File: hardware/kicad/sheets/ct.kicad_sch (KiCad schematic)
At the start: 31 parts, among them J12 CT, J13 AC_SENSE_DNP, U7 ADE7953ACPZ, Y1 3.579545MHz XO

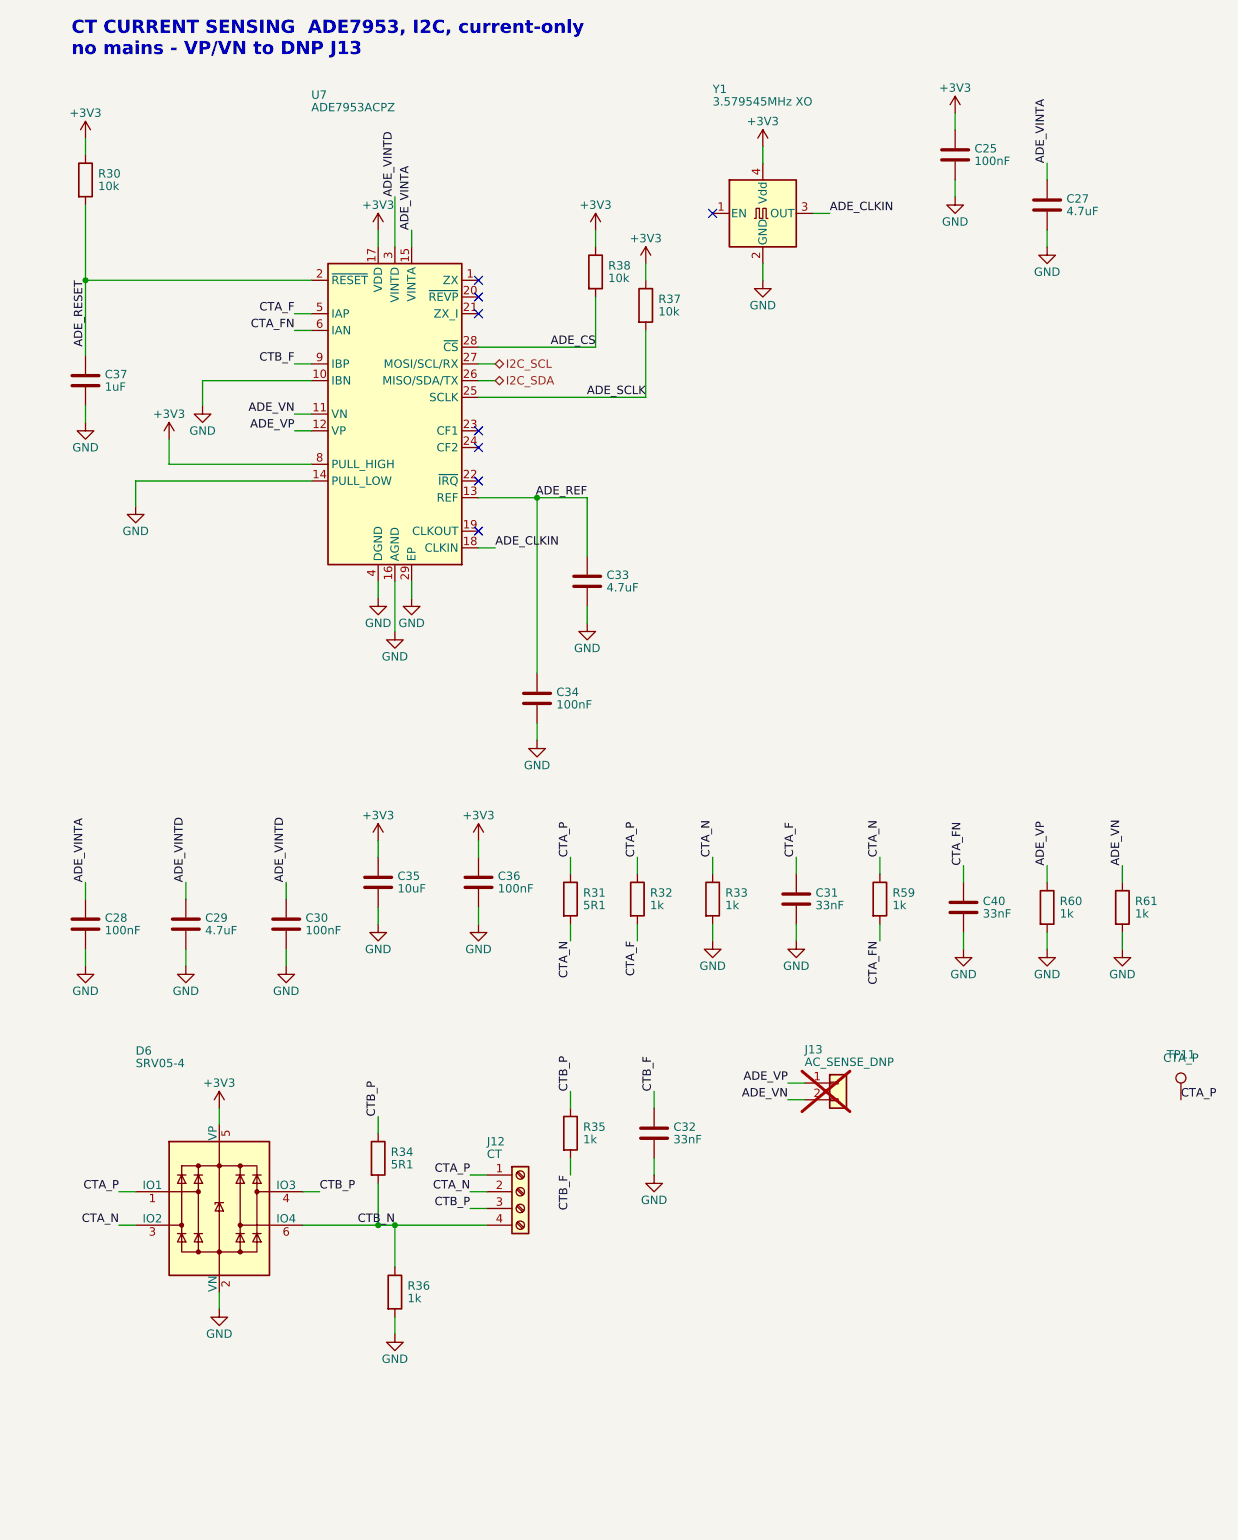
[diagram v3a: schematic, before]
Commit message: hardware: inline front-ends and decoupling at the pins (review 12, 13)
Fourth batch from SCHEMATIC-REVIEW-2026-10-22.md.

Thermocouples: each MAX31856 front-end is an inline chain - the terminal
mirrored so its pins face the IC, K+ and K- on two lines through their
100R, the 100 nF differential cap bridging the lines, the 10 nF caps to
GND off each line, BIAS returned to the raw K- node along the bottom -
and AVDD/DVDD rise to a short +3V3 rail with both 100 nF hanging from
it. The ICs slid 7.62 mm right to make room; nothing else moved.

CT: J12 feeds four lines at 17.78 mm pitch with the 5R1 burden between
each pair, the 1k series parts in the path, the 33 nF to GND off each
filtered node and the 1k references off the N lines; the filtered nodes
end in the CTA_F / CTA_FN / CTB_F labels the ADE7953 pins already
carried. D6 keeps a label-fed clamp block beside the chain. VDD, VINTD
and VINTA each get a rail at the IC's top pin with their two caps on it;
R37/R38 moved 7.62 mm right to clear them.

io: IN1-IN3 are three identical rows - J11 mirrored, 1k in the path, the
10k pull-up above and 100 nF below the node, the hierarchical label at
the end - with D5's clamp block below them.

mcu: C6/C7 hang from U1's 3V3 pin. power: U2 is drawn as an inline
5 V -> 3.3 V chain with C1/C2 on its input and C3/C4 on its output in
the row the caps already occupied; LED2/R9 slid right.

Every pin landed on wiring by construction (the geometry helper checks
each symbol's pins against the wires), ERC is clean, the layout checker
reports no overlaps, the netlist still has 108 nets and the board sync
re-netted nothing. Fab outputs regenerated (schematic PDF, timestamps).

Co-Authored-By: Claude Fable 5.1 <noreply@anthropic.com>
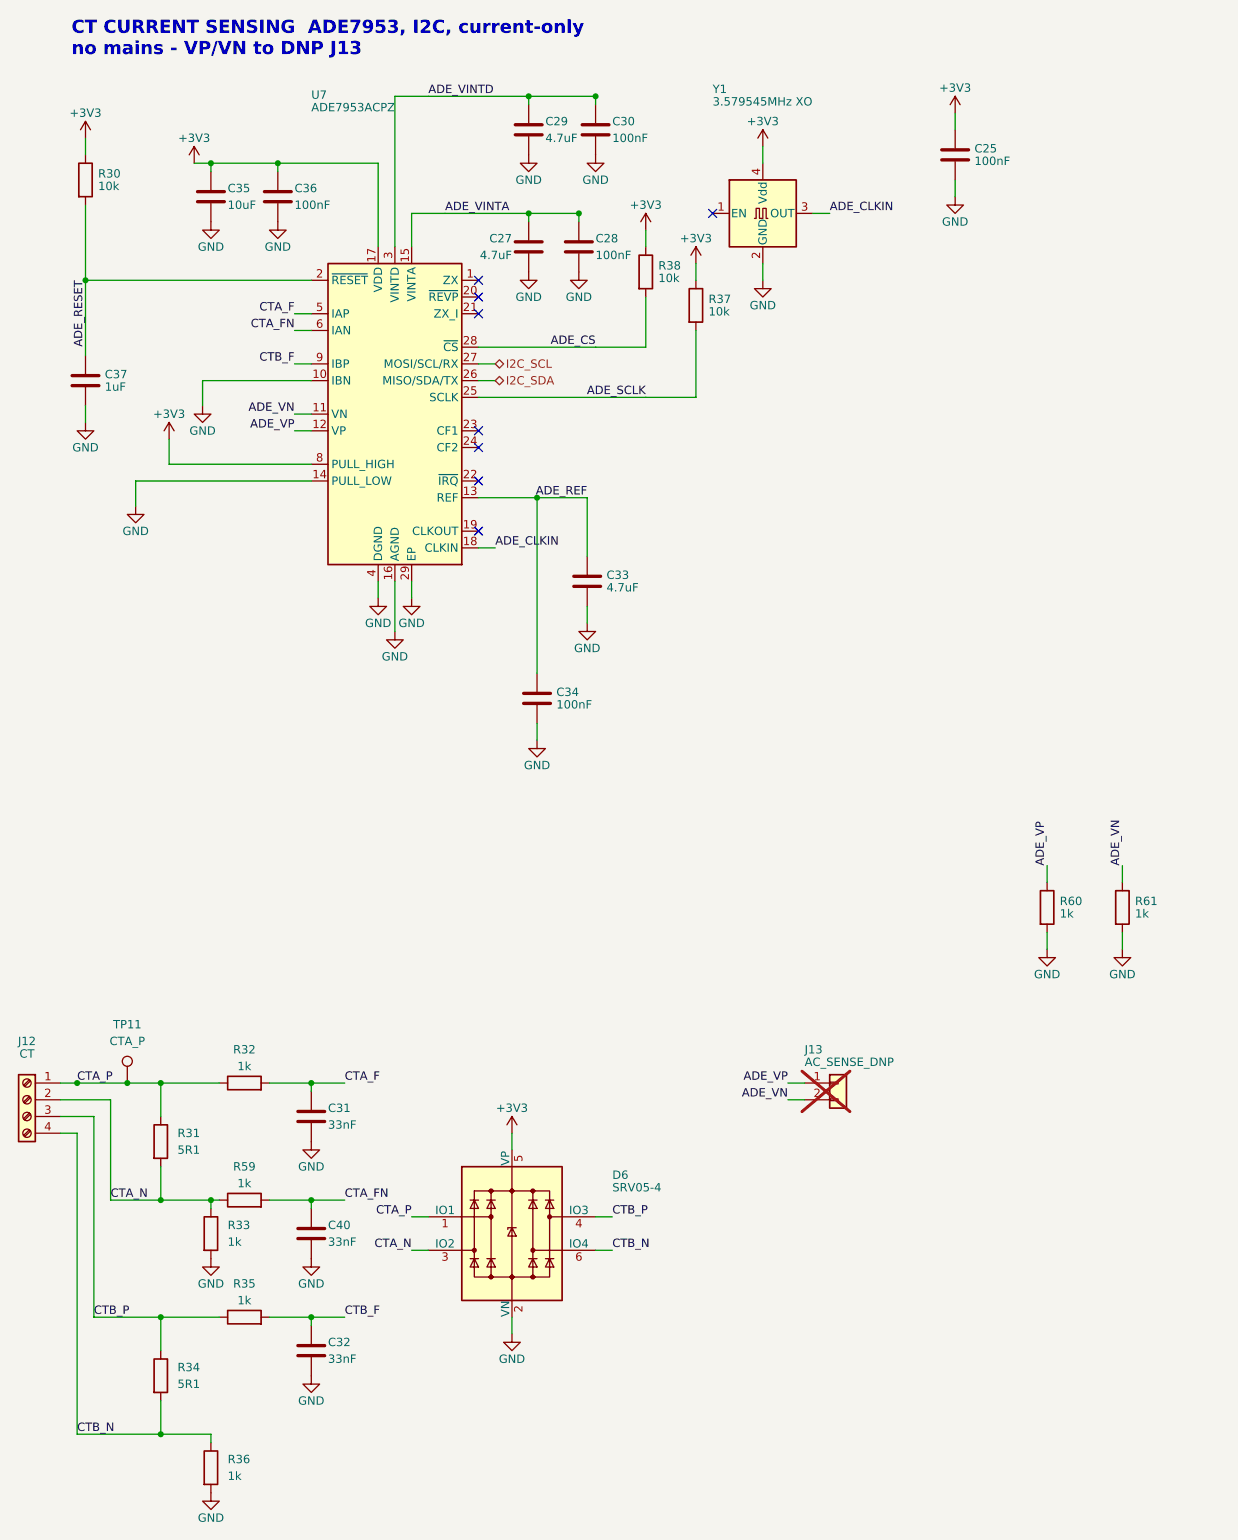
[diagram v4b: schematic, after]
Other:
- moved on the sheet: C27, C28, C29, C30, C31, C32, C35, C36, C40, D6, J12, R31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

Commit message: hardware: drop the five test points a connector already exposes
TP1 (+3V3), TP2 (+5V), TP7/TP8 (I2C) and TP11 (CTA_P) each sat on a net
that a connector pin already reaches: +3V3 and I2C on the J7 AUX header
and J14 QWIIC, +5V on J5 pin 1, CTA_P on J12 pin 1. They are gone from
the test, mcu and ct sheets (TP3 and TP9/TP10 slide left into the gaps),
the board is synced, and the copper that only existed to reach them is
removed: eight segments and one via, 15.5 mm in all, most of it +5V's
spur from U2.3 up to the old TP2. DRC is 0 violations / 0 unconnected
with every severity on.

The seven that remain (TP3-TP6, TP9, TP10, TP12) probe nets nothing else
reaches, and none moved: on the board each already sits inline on its
net's route with at most a 0.4 mm jog. TP12 is the one with a real stub
(3.3 mm from R46.2), and SJ2's courtyard is what keeps it there.

TP_LEGEND_OK is empty again - dropping TP11 was the way out review A2
named. README, the bench smoke test (rails now probed at C2 / J7 pin 1),
gen_jlc's not-assembled set and the datasheet manifest follow. ERC 0,
make pcb-check ALL CHECKS PASS, SYNC IDEMPOTENT: PASS; fab outputs and
3D renders regenerated.

Co-Authored-By: Claude Fable 5.1 <noreply@anthropic.com>
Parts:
- removed TP11: CTA_P, TestPoint:TestPoint_Pad_D1.0mm, symbol Connector:TestPoint
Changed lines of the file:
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@@
-	)
-	(junction
-		(at 30.48 187.96)
-		(diameter 0)
-		(color 0 0 0 0)
 	)
 	(junction
@@
 					(unit 1)
 				)
-			)
-		)
-	)
-	(symbol
-		(lib_id "Connector:TestPoint")
-		(at 30.48 187.96 0)
-		(unit 1)
-		(body_style 1)
-		(exclude_from_sim no)
-		(in_bom yes)
-		(on_board yes)
-		(in_pos_files yes)
-		(dnp no)
-		(property "Reference" "TP11"
-			(at 30.48 179.07 0)
-			(show_name no)
-			(do_not_autoplace no)
-			(effects
-				(font
-					(size 1.27 1.27)
-				)
-			)
-		)
-		(property "Value" "CTA_P"
-			(at 30.48 181.61 0)
-			(show_name no)
-			(do_not_autoplace no)
-			(effects
-				(font
-					(size 1.27 1.27)
-				)
-			)
-		)
-		(property "Footprint" "TestPoint:TestPoint_Pad_D1.0mm"
-			(at 30.48 187.96 0)
-			(hide yes)
-			(show_name no)
-			(do_not_autoplace no)
-			(effects
-				(font
-					(size 1.27 1.27)
-				)
-			)
-		)
-		(property "Datasheet" ""
-			(at 30.48 187.96 0)
-			(hide yes)
-			(show_name no)
-			(do_not_autoplace no)
-			(effects
-				(font
-					(size 1.27 1.27)
-				)
-			)
-		)
-		(property "Description" "test point"
-			(at 30.48 187.96 0)
-			(hide yes)
-			(show_name no)
-			(do_not_autoplace no)
-			(effects
-				(font
-					(size 1.27 1.27)
-				)
-			)
-		)
-		(pin "1"
-		)
-		(instances
-			(project ""
-				(path "/9f5a642e-6117-5c0b-a848-1913aa103515"
-					(reference "TP11")
-					(unit 1)
-				)

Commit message: hardware: drop J13, the DNP header on the ADE7953 voltage channel
True power measurement is not a planned feature, so the provision for a
future off-board isolated AC-sense accessory goes: J13 is removed from
the ct sheet, VP/VN stay held at GND by R60/R61 and reach nothing else,
and the sheet note says so. gen_jlc.DNP is empty; J13 leaves
NOT_ASSEMBLED, the silk legend tables and the datasheet manifest, and
README/DESIGN-NOTES no longer describe the header or the upgrade path.

On the board the header's two through-hole pads were also the layer
change in each net's route, so removing the footprint left ADE_VP and
ADE_VN each split between F.Cu and B.Cu. A 0.6/0.3 via now sits where
each pad was, and the zones are refilled around them. DRC 0 violations
/ 0 unconnected with every severity on, ERC 0, make pcb-check ALL
CHECKS PASS, SYNC IDEMPOTENT: PASS; fab outputs and 3D renders
regenerated.

Co-Authored-By: Claude Fable 5.1 <noreply@anthropic.com>
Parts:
- removed J13: AC_SENSE_DNP, Connector_PinHeader_2.54mm:PinHeader_1x02_P2.54mm_Vertical, symbol Connector_Generic:Conn_01x02
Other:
- note added: "CT CURRENT SENSING ADE7953, I2C, current-only no mains - VP/VN held at GND by R60/R61"
- note removed: "CT CURRENT SENSING ADE7953, I2C, current-only no mains - VP/VN to DNP J13"
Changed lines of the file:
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@@
 		(comment 2 "4-layer, 100 x 100 mm, JLCPCB standard process")
 	)
-	(text "CT CURRENT SENSING  ADE7953, I2C, current-only\nno mains - VP/VN to DNP J13"
+	(text "CT CURRENT SENSING  ADE7953, I2C, current-only\nno mains - VP/VN held at GND by R60/R61"
 		(exclude_from_sim no)
 		(at 22 29.4 0)
@@
 	(wire
 		(pts
-			(xy 133.35 187.96) (xy 130.81 187.96)
-		)
-		(stroke
-			(width 0)
-			(type default)
-		)
-	)
-	(wire
-		(pts
 			(xy 35.56 236.22) (xy 35.56 241.3)
 		)
@@
 	(wire
 		(pts
-			(xy 133.35 190.5) (xy 130.81 190.5)
-		)
-		(stroke
-			(width 0)
-			(type default)
-		)
-	)
-	(wire
-		(pts
 			(xy 58.42 93.98) (xy 36.83 93.98)
 		)
@@
 		)
 	)
-	(label "ADE_VP"
-		(at 130.81 187.96 180)
-		(effects
-			(font
-				(size 1.27 1.27)
-			)
-			(justify right bottom)
-		)
-	)
 	(label "ADE_REF"
 		(at 100.33 99.06 180)
@@
 		)
 	)
-	(label "ADE_VN"
-		(at 130.81 190.5 180)
-		(effects
-			(font
-				(size 1.27 1.27)
-			)
-			(justify right bottom)
-		)
-	)
 	(label "CTA_F"
 		(at 63.5 187.96 0)
@@
 					(unit 1)
 				)
-			)
-		)
-	)
-	(symbol
-		(lib_id "Connector_Generic:Conn_01x02")
-		(at 138.43 187.96 0)
-		(unit 1)
-		(body_style 1)
-		(exclude_from_sim no)
-		(in_bom yes)
-		(on_board yes)
-		(in_pos_files yes)
-		(dnp yes)
-		(property "Reference" "J13"
-			(at 133.35 182.88 0)
-			(show_name no)
-			(do_not_autoplace no)
-			(effects
-				(font
-					(size 1.27 1.27)
-				)
-				(justify left)
-			)
-		)
-		(property "Value" "AC_SENSE_DNP"
-			(at 133.35 184.78 0)
-			(show_name no)
-			(do_not_autoplace no)
-			(effects
-				(font
-					(size 1.27 1.27)
-				)
-				(justify left)
-			)
-		)
-		(property "Footprint" "Connector_PinHeader_2.54mm:PinHeader_1x02_P2.54mm_Vertical"
-			(at 138.43 187.96 0)
-			(hide yes)
-			(show_name no)
-			(do_not_autoplace no)
-			(effects
-				(font
-					(size 1.27 1.27)
-				)
-			)
-		)
-		(property "Datasheet" ""
-			(at 138.43 187.96 0)
-			(hide yes)
-			(show_name no)
-			(do_not_autoplace no)
-			(effects
-				(font
-					(size 1.27 1.27)
-				)
-			)
-		)
-		(property "Description" "Generic connector, single row, 01x02, script generated (kicad-library-utils/schlib/autogen/connector/)"
-			(at 138.43 187.96 0)
-			(hide yes)
-			(show_name no)
-			(do_not_autoplace no)
-			(effects
-				(font
-					(size 1.27 1.27)
-				)
-			)
-		)
-		(pin "1"
-		)
-		(pin "2"
-		)
-		(instances
-			(project "bisque-controller"
-				(path "/f24e0cd2-71c5-510c-9d15-562ab64c4388/6c704e24-0c23-5bb2-a84e-a8ccbf5f5ca5"
-					(reference "J13")
-					(unit 1)
-				)

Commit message: hardware: the five quick fixes from the 2026-10-05/10-22 reviews
Schematic (rev B.3, sheets ct/power/mcu/ssr + root):
- R65, 1k from CTA_P to GND, mirrors R33 so the floating CT secondary
  sits at +-V/2 on IAP/IAN and channel A's pin limit is 139 A nominal,
  the same as channel B (schematic review 10-05 item 2).
- D9/D10 freewheel diodes are B5819W (JSCJ C8598, Basic, 1 A / 40 V,
  9 A surge) in the same SOD-123 land, replacing the 1N4148W whose
  150 mA rating never covered a 200 mA contactor coil (PCB review 10-05
  item 12). The SS34 was tried first and does not fit the SSR column.
- ADE_RESET is a hierarchical net to U1 IO37, the spare GPIO; the R30/C37
  RC stays for the power-on stretch (10-22 review E3).
- PWR_STATUS: BUCK_5V through R66 (100k) over R67+R68 (130k) to U1 IO45,
  2.8 V when the 24 V buck runs and 0 V on USB only (10-22 review E4).
  The TPS2116 ST pin would have said the same thing but its pad is boxed
  in by the USB pair on this layout, so it stays unconnected (C3, rev C).

Board:
- Every +5V layer transition (7) now has a second 0.6/0.3 via 0.85 mm
  away with a stub on each layer; the two in the USB corner use 0.3 mm
  stubs (fab-readiness C, "attempted, not landed" -> fixed).
- R65 placed below the CT filters; the divider in the two free columns
  south of U1, lifted 0.75 mm so the nameplate pocket keeps its 16.2 mm
  (it prints at 62% now). BUCK_5V tap hand-routed, the rest by the
  in-house router. DRC 0, make pcb-check ALL CHECKS PASS, 3D re-rendered.

Firmware/docs: KILN_PIN_ADE_RESET (37) and KILN_PIN_PWR_STATUS (45) in
Kconfig with the GPIO45 strapping caveat, check_pinmap NET_KCONFIG,
docs/pin-assignments.md (all 30 GPIOs assigned), DESIGN-NOTES sections
for each change, status notes in the four review documents, gen_jlc
sourcing + JLC_PLACEMENT rows, lcsc_pads cache and datasheet manifest.

Co-Authored-By: Claude Fable 5.1 <noreply@anthropic.com>
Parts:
- added R65: 1k, Resistor_SMD:R_0805_2012Metric, symbol Device:R
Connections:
- net CTA_P: now also R65.2
- net GND: now also R65.1
